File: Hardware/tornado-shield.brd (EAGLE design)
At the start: 84.9 x 84 mm, 32 parts, among them CON1 ROV_SHIELD_V2, Q1 DMP2012SN-7, U1 LM2678S-5.0, U2 LM3409HV'LM3409HV'

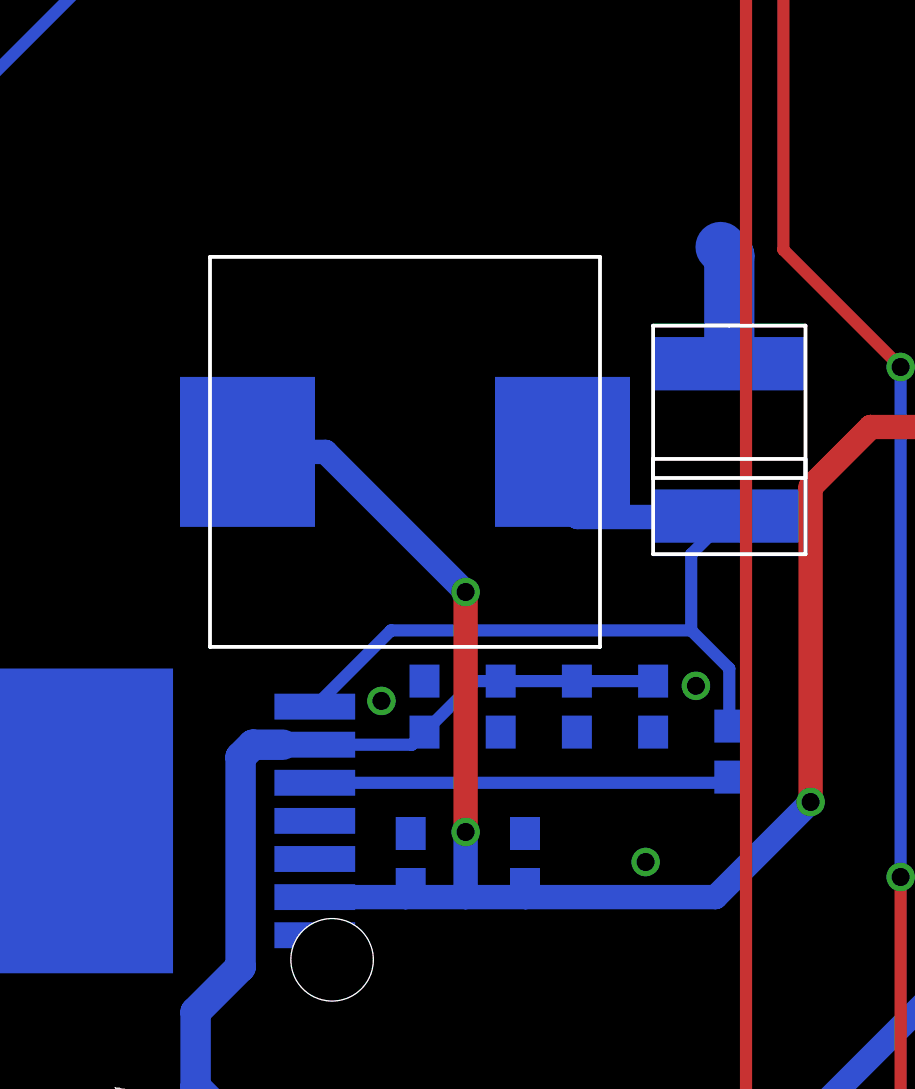
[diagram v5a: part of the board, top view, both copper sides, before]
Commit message: Fixed small problem with buck layout
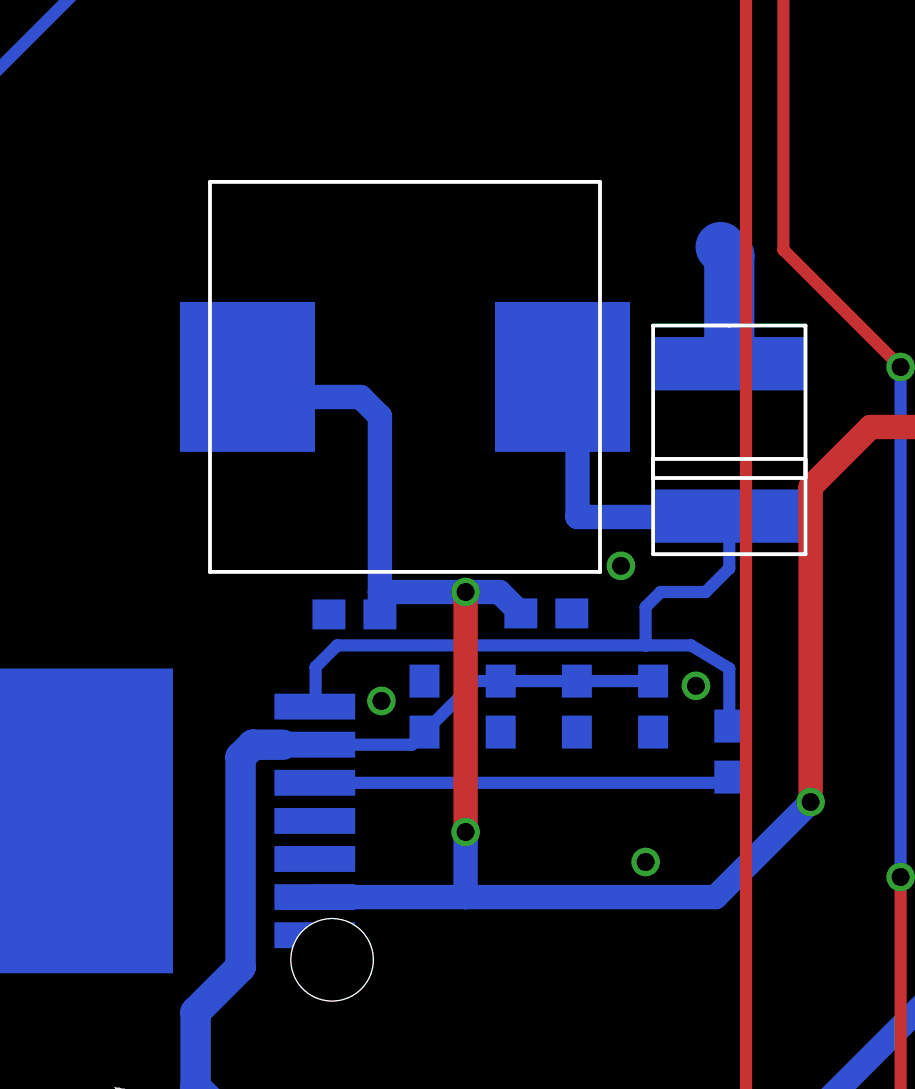
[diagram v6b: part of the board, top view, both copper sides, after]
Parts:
- moved C2 8.37 mm to (21.8, 30.3), turned to 0 degrees
- moved C3 8.22 mm to (28.2, 30.3), turned to 180 degrees
- moved L1 2.50 mm to (23.5, 38.2)
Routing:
- net +5V: track 184.2 -> 190.6 mm
- net SWOUT: track 29.0 -> 34.2 mm
- net GND: vias 6 -> 7
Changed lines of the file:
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@@
 <attribute name="VALUE" x="32.385" y="25.045" size="1.27" layer="28" rot="MR90"/>
 </element>
-<element name="C2" library="rcl" package="C0603" value="180uF" x="23.67" y="22.1" smashed="yes" rot="MR90">
-<attribute name="NAME" x="23.035" y="17.655" size="1.27" layer="26" rot="MR90"/>
-<attribute name="VALUE" x="23.035" y="15.115" size="1.27" layer="28" rot="MR90"/>
-</element>
-<element name="C3" library="rcl" package="C0603" value="180uF" x="27.48" y="22.1" smashed="yes" rot="MR90">
-<attribute name="NAME" x="26.845" y="17.655" size="1.27" layer="26" rot="MR90"/>
-<attribute name="VALUE" x="28.115" y="15.115" size="1.27" layer="28" rot="MR90"/>
+<element name="C2" library="rcl" package="C0603" value="180uF" x="21.79395" y="30.25255" smashed="yes" rot="MR0">
+<attribute name="NAME" x="20.23895" y="29.61755" size="1.27" layer="26" rot="MR0"/>
+<attribute name="VALUE" x="28.77895" y="29.61755" size="1.27" layer="28" rot="MR0"/>
+</element>
+<element name="C3" library="rcl" package="C0603" value="180uF" x="28.18965" y="30.2876" smashed="yes" rot="MR180">
+<attribute name="NAME" x="29.74465" y="30.4226" size="1.27" layer="26" rot="MR180"/>
+<attribute name="VALUE" x="21.20465" y="29.6526" size="1.27" layer="28" rot="MR180"/>
 </element>
 <element name="C4" library="rcl" package="C0603" value="15uF" x="24.13" y="27.18" smashed="yes" rot="MR90">
@@
 </element>
 <element name="C5" library="rcl" package="C0603" value="15uF" x="26.67" y="27.18" smashed="yes" rot="MR270">
-<attribute name="NAME" x="27.305" y="31.625" size="1.27" layer="26" rot="MR270"/>
+<attribute name="NAME" x="25.805" y="25.625" size="1.27" layer="26" rot="MR270"/>
 <attribute name="VALUE" x="26.035" y="32.895" size="1.27" layer="28" rot="MR270"/>
 </element>
 <element name="C6" library="rcl" package="C0603" value="15uF" x="29.21" y="27.18" smashed="yes" rot="MR270">
-<attribute name="NAME" x="29.845" y="31.625" size="1.27" layer="26" rot="MR270"/>
+<attribute name="NAME" x="29.845" y="25.625" size="1.27" layer="26" rot="MR270"/>
 <attribute name="VALUE" x="29.845" y="25.275" size="1.27" layer="28" rot="MR270"/>
 </element>
 <element name="C7" library="rcl" package="C0603" value=".47uF" x="31.75" y="27.18" smashed="yes" rot="MR270">
-<attribute name="NAME" x="32.385" y="31.625" size="1.27" layer="26" rot="MR270"/>
+<attribute name="NAME" x="32.385" y="25.125" size="1.27" layer="26" rot="MR270"/>
 <attribute name="VALUE" x="32.385" y="25.275" size="1.27" layer="28" rot="MR270"/>
 </element>
 <element name="U$3" library="samssuperhot" package="DO-214AB" value="SK1545-TP" x="34.29" y="36.07" smashed="yes" rot="MR270"/>
-<element name="L1" library="samssuperhot" package="7443551221" value="22uH" x="23.48" y="35.67" smashed="yes" rot="MR0"/>
+<element name="L1" library="samssuperhot" package="7443551221" value="22uH" x="23.48" y="38.17" smashed="yes" rot="MR0"/>
 <element name="R_UV2" library="DiscreteComponents" package="R0603" value="13700" x="45.72" y="48.26" smashed="yes" rot="MR180">
 <attribute name="NAME" x="38.1" y="48.895" size="1.27" layer="26" rot="MR180"/>
@@
 <wire x1="34.29" y1="38.61" x2="34.29" y2="42.21" width="1.6764" layer="16"/>
 <wire x1="34.29" y1="42.21" x2="34" y2="42.5" width="1.6764" layer="16"/>
+<via x="30.6778" y="31.873" extent="1-16" drill="0.6"/>
 </signal>
 <signal name="+12V">
@@
 <contactref element="U$3" pad="P$2"/>
 <contactref element="L1" pad="P$1"/>
-<wire x1="20.4724" y1="27.18" x2="23.0124" y2="29.72" width="0.4064" layer="16"/>
-<wire x1="23.0124" y1="29.72" x2="33.02" y2="29.72" width="0.4064" layer="16"/>
-<wire x1="34.29" y1="33.53" x2="33.02" y2="32.26" width="0.4064" layer="16"/>
-<wire x1="33.02" y1="32.26" x2="33.02" y2="29.72" width="0.4064" layer="16"/>
+<wire x1="21.22" y1="29.22" x2="31.5" y2="29.22" width="0.4064" layer="16"/>
+<wire x1="31.5" y1="29.22" x2="33.02" y2="29.22" width="0.4064" layer="16"/>
 <wire x1="34.29" y1="26.53" x2="34.29" y2="28.45" width="0.4064" layer="16"/>
-<wire x1="34.29" y1="28.45" x2="33.02" y2="29.72" width="0.4064" layer="16"/>
-<wire x1="28.73" y1="35.67" x2="29.23" y2="33.5" width="0.8128" layer="16"/>
+<wire x1="34.29" y1="28.45" x2="33.02" y2="29.22" width="0.4064" layer="16"/>
 <wire x1="29.23" y1="33.5" x2="33.5" y2="33.5" width="0.8128" layer="16"/>
 <wire x1="33.5" y1="33.5" x2="33.5" y2="33.53" width="0.8128" layer="16"/>
 <wire x1="33.5" y1="33.53" x2="34.29" y2="33.53" width="0.8128" layer="16"/>
+<wire x1="28.73" y1="38.17" x2="29.23" y2="38.17" width="0.8128" layer="16"/>
+<wire x1="29.23" y1="38.17" x2="29.23" y2="33.5" width="0.8128" layer="16"/>
+<wire x1="21.22" y1="29.22" x2="20.5" y2="28.5" width="0.4064" layer="16"/>
+<wire x1="20.5" y1="28.5" x2="20.5" y2="27.2076" width="0.4064" layer="16"/>
+<wire x1="20.5" y1="27.2076" x2="20.4724" y2="27.18" width="0.4064" layer="16"/>
+<wire x1="34.29" y1="33.53" x2="34.29" y2="31.79" width="0.4064" layer="16"/>
+<wire x1="34.29" y1="31.79" x2="33.5" y2="31" width="0.4064" layer="16"/>
+<wire x1="33.5" y1="31" x2="32" y2="31" width="0.4064" layer="16"/>
+<wire x1="32" y1="31" x2="31.5" y2="30.5" width="0.4064" layer="16"/>
+<wire x1="31.5" y1="30.5" x2="31.5" y2="29.22" width="0.4064" layer="16"/>
 </signal>
 <signal name="+5V">
@@
 <wire x1="81" y1="63.5" x2="82.5" y2="65" width="0.8128" layer="1"/>
 <wire x1="39" y1="36.5" x2="72.5" y2="36.5" width="0.8128" layer="1"/>
-<wire x1="20.4724" y1="20.83" x2="23.5" y2="20.83" width="0.8128" layer="16"/>
-<wire x1="23.5" y1="20.83" x2="25.5" y2="20.83" width="0.8128" layer="16"/>
-<wire x1="25.5" y1="20.83" x2="27.5" y2="20.83" width="0.8128" layer="16"/>
-<wire x1="27.5" y1="20.83" x2="33.83" y2="20.83" width="0.8128" layer="16"/>
+<wire x1="20.4724" y1="20.83" x2="25.5" y2="20.83" width="0.8128" layer="16"/>
+<wire x1="25.5" y1="20.83" x2="33.83" y2="20.83" width="0.8128" layer="16"/>
 <wire x1="33.83" y1="20.83" x2="37" y2="24" width="0.8128" layer="16"/>
 <via x="37" y="24" extent="1-16" drill="0.6"/>
 <wire x1="37" y1="24" x2="37" y2="34.5" width="0.8128" layer="1"/>
 <wire x1="37" y1="34.5" x2="39" y2="36.5" width="0.8128" layer="1"/>
-<wire x1="23.67" y1="21.25" x2="23.67" y2="21" width="0.8128" layer="16"/>
-<wire x1="23.67" y1="21" x2="23.5" y2="20.83" width="0.8128" layer="16"/>
-<wire x1="27.48" y1="21.25" x2="27.48" y2="20.85" width="0.8128" layer="16"/>
-<wire x1="27.48" y1="20.85" x2="27.5" y2="20.83" width="0.8128" layer="16"/>
-<wire x1="18.23" y1="35.67" x2="20.83" y2="35.67" width="0.8128" layer="16"/>
-<wire x1="20.83" y1="35.67" x2="25.5" y2="31" width="0.8128" layer="16"/>
 <via x="25.5" y="31" extent="1-16" drill="0.6"/>
 <wire x1="25.5" y1="31" x2="25.5" y2="23" width="0.8128" layer="1"/>
 <via x="25.5" y="23" extent="1-16" drill="0.6"/>
 <wire x1="25.5" y1="23" x2="25.5" y2="20.83" width="0.8128" layer="16"/>
+<wire x1="25.5" y1="31" x2="22.64395" y2="31" width="0.8128" layer="16"/>
+<wire x1="22.64395" y1="31" x2="22.64395" y2="30.25255" width="0.8128" layer="16"/>
+<wire x1="22.64395" y1="31" x2="22.64395" y2="36.85605" width="0.8128" layer="16"/>
+<wire x1="22.64395" y1="36.85605" x2="22" y2="37.5" width="0.8128" layer="16"/>
+<wire x1="22" y1="37.5" x2="18.9" y2="37.5" width="0.8128" layer="16"/>
+<wire x1="18.9" y1="37.5" x2="18.23" y2="38.17" width="0.8128" layer="16"/>
+<wire x1="27.33965" y1="30.2876" x2="26.62725" y2="31" width="0.8128" layer="16"/>
+<wire x1="26.62725" y1="31" x2="25.5" y2="31" width="0.8128" layer="16"/>
 </signal>
 <signal name="N$2">

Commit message: Added Status LEDs for power and Solenoids
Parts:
- added PWR_ON, SOL1_STAT, SOL2_STAT: (no value), eagle-ltspice:LED_SML0603
- added R3, R4, R5: (no value), rcl:R0603
- R1, R2: device rcl:R1206 -> rcl:R0603
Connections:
- new net N$12: PWR_ON.C, R5.2
- new net N$9: R4.2, SOL1_STAT.C
- new net SOL2_STAT: R3.2, SOL2_STAT.C
- net +5V: now also PWR_ON.A
- net GND: now also R3.1, R4.1, R5.1
- net SOL_O1: now also SOL1_STAT.A
- net SOL_O2: now also SOL2_STAT.A
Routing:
- net +5V: track 190.6 -> 196.7 mm, vias 3 -> 4
- net N$12: track 0.00 -> 4.40 mm, vias 0 -> 1
- net SOL2_STAT: track 0.00 -> 3.79 mm, vias 0 -> 1
- net N$9: track 0.00 -> 3.73 mm, vias 0 -> 1
- net SOL_O1: track 61.8 -> 64.6 mm
- net SOL_O2: track 40.6 -> 42.4 mm
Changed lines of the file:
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@@
 <element name="U$4" library="samssuperhot" package="DO-214AB" value="SK1545-TP" x="11.43" y="55.38" smashed="yes" rot="MR180"/>
 <element name="U$5" library="samssuperhot" package="DO-214AB" value="SK1545-TP" x="11.43" y="70.35" smashed="yes" rot="MR180"/>
-<element name="R2" library="rcl" package="R1206" value="" x="3.81" y="67.31" smashed="yes" rot="MR180">
+<element name="R2" library="rcl" package="R0603" value="" x="3.81" y="67.31" smashed="yes" rot="MR180">
 <attribute name="NAME" x="2.54" y="66.04" size="1.27" layer="26" rot="MR180"/>
 <attribute name="VALUE" x="2.54" y="69.85" size="1.27" layer="28" rot="MR180"/>
 </element>
-<element name="R1" library="rcl" package="R1206" value="" x="3.81" y="54.61" smashed="yes" rot="MR180">
+<element name="R1" library="rcl" package="R0603" value="" x="3.81" y="54.61" smashed="yes" rot="MR180">
 <attribute name="NAME" x="2.54" y="53.34" size="1.27" layer="26" rot="MR180"/>
 <attribute name="VALUE" x="2.54" y="57.15" size="1.27" layer="28" rot="MR180"/>
@@
 <attribute name="VALUE" x="29.595" y="61.365" size="1.27" layer="28" rot="MR90"/>
 </element>
+<element name="PWR_ON" library="eagle-ltspice" package="LED_SML0603" value="" x="27.5" y="16" smashed="yes" rot="R90">
+<attribute name="SPICEPREFIX" value="D" x="27.5" y="16" size="1.778" layer="27" rot="R90" display="off"/>
+<attribute name="SPICETYPE" value="diode" x="27.5" y="16" size="1.778" layer="27" rot="R90" display="off"/>
+<attribute name="SPICEMODEL" value="NONE" x="27.5" y="16" size="1.778" layer="27" rot="R90" display="off"/>
+<attribute name="NAME" x="22" y="13" size="1.27" layer="25"/>
+<attribute name="VALUE" x="29.5" y="15" size="1.27" layer="27" rot="R90"/>
+</element>
+<element name="SOL1_STAT" library="eagle-ltspice" package="LED_SML0603" value="" x="4" y="60.5" smashed="yes" rot="R90">
+<attribute name="SPICEPREFIX" value="D" x="4" y="60.5" size="1.778" layer="27" rot="R90" display="off"/>
+<attribute name="SPICETYPE" value="diode" x="4" y="60.5" size="1.778" layer="27" rot="R90" display="off"/>
+<attribute name="SPICEMODEL" value="NONE" x="4" y="60.5" size="1.778" layer="27" rot="R90" display="off"/>
+<attribute name="NAME" x="3" y="59.5" size="1.27" layer="25" rot="R90"/>
+<attribute name="VALUE" x="6" y="59.5" size="1.27" layer="27" rot="R90"/>
+</element>
+<element name="SOL2_STAT" library="eagle-ltspice" package="LED_SML0603" value="" x="18.5" y="76" smashed="yes" rot="R270">
+<attribute name="SPICEPREFIX" value="D" x="18.5" y="76" size="1.778" layer="27" rot="R270" display="off"/>
+<attribute name="SPICETYPE" value="diode" x="18.5" y="76" size="1.778" layer="27" rot="R270" display="off"/>
+<attribute name="SPICEMODEL" value="NONE" x="18.5" y="76" size="1.778" layer="27" rot="R270" display="off"/>
+<attribute name="NAME" x="14" y="73" size="1.27" layer="25"/>
+<attribute name="VALUE" x="16.5" y="77" size="1.27" layer="27" rot="R270"/>
+</element>
+<element name="R3" library="rcl" package="R0603" value="" x="19" y="79" rot="MR0"/>
+<element name="R4" library="rcl" package="R0603" value="" x="4" y="56.5" rot="MR0"/>
+<element name="R5" library="rcl" package="R0603" value="" x="31" y="13.5" rot="MR0"/>
 </elements>
 <signals>
@@
 <wire x1="34.29" y1="42.21" x2="34" y2="42.5" width="1.6764" layer="16"/>
 <via x="30.6778" y="31.873" extent="1-16" drill="0.6"/>
+<contactref element="R3" pad="1"/>
+<contactref element="R4" pad="1"/>
+<contactref element="R5" pad="1"/>
 </signal>
 <signal name="+12V">
@@
 <wire x1="27.33965" y1="30.2876" x2="26.62725" y2="31" width="0.8128" layer="16"/>
 <wire x1="26.62725" y1="31" x2="25.5" y2="31" width="0.8128" layer="16"/>
+<contactref element="PWR_ON" pad="A"/>
+<wire x1="25.5" y1="20.83" x2="27.5" y2="20.83" width="0.4064" layer="16"/>
+<wire x1="27.5" y1="20.83" x2="27.5" y2="19" width="0.4064" layer="16"/>
+<via x="27.5" y="19" extent="1-16" drill="0.6"/>
+<wire x1="27.5" y1="19" x2="27.5" y2="16.75" width="0.4064" layer="1"/>
 </signal>
 <signal name="N$2">
@@
 <wire x1="8.83" y1="55.88" x2="8.89" y2="55.38" width="0.4064" layer="16"/>
 <wire x1="8.89" y1="55.38" x2="8.89" y2="54.61" width="0.4064" layer="16"/>
-<wire x1="8.89" y1="54.61" x2="5.232" y2="54.61" width="0.4064" layer="16"/>
+<wire x1="8.89" y1="54.61" x2="4.66" y2="54.61" width="0.4064" layer="16"/>
 <wire x1="8.83" y1="61.595" x2="5.905" y2="61.595" width="0.4064" layer="16"/>
 <wire x1="5.905" y1="61.595" x2="4" y2="63.5" width="0.4064" layer="16"/>
@@
 <wire x1="12.5" y1="81.5" x2="32.06" y2="81.5" width="0.4064" layer="1"/>
 <wire x1="32.06" y1="81.5" x2="35.21" y2="78.35" width="0.4064" layer="1"/>
+<contactref element="SOL1_STAT" pad="A"/>
+<wire x1="4" y1="61.25" x2="4" y2="63.5" width="0.4064" layer="1"/>
 </signal>
 <signal name="GPIO2">
@@
 <wire x1="8.83" y1="64.135" x2="6.985" y2="64.135" width="0.4064" layer="16"/>
 <wire x1="6.985" y1="64.135" x2="5.232" y2="65.888" width="0.4064" layer="16"/>
-<wire x1="5.232" y1="65.888" x2="5.232" y2="67.31" width="0.4064" layer="16"/>
-<wire x1="5.232" y1="67.31" x2="7.772" y2="69.85" width="0.4064" layer="16"/>
+<wire x1="5.232" y1="65.888" x2="4.66" y2="67.31" width="0.4064" layer="16"/>
+<wire x1="4.66" y1="67.31" x2="7.772" y2="69.85" width="0.4064" layer="16"/>
 <wire x1="7.772" y1="69.85" x2="8.89" y2="70.35" width="0.4064" layer="16"/>
 <wire x1="8.89" y1="70.35" x2="8.89" y2="72.89" width="0.4064" layer="16"/>
 <wire x1="8.89" y1="72.89" x2="10" y2="74" width="0.4064" layer="16"/>
 <via x="10" y="74" extent="1-16" drill="0.6"/>
-<wire x1="10" y1="74" x2="33.4" y2="74" width="0.4064" layer="1"/>
+<wire x1="10" y1="74" x2="18.5" y2="74" width="0.4064" layer="1"/>
+<wire x1="18.5" y1="74" x2="33.4" y2="74" width="0.4064" layer="1"/>
 <wire x1="33.4" y1="74" x2="35.21" y2="75.81" width="0.4064" layer="1"/>
+<contactref element="SOL2_STAT" pad="A"/>
+<wire x1="18.5" y1="75.25" x2="18.5" y2="74" width="0.4064" layer="1"/>
 </signal>
 <signal name="GPIO3">
@@
 <signal name="N$6">
 </signal>
+<signal name="SOL2_STAT">
+<contactref element="SOL2_STAT" pad="C"/>
+<contactref element="R3" pad="2"/>
+<wire x1="18.5" y1="76.75" x2="17.75" y2="76.75" width="0.4064" layer="1"/>
+<wire x1="17.75" y1="76.75" x2="17" y2="77.5" width="0.4064" layer="1"/>
+<wire x1="18.15" y1="79" x2="17" y2="77.85" width="0.4064" layer="16"/>
+<wire x1="17" y1="77.85" x2="17" y2="77.5" width="0.4064" layer="16"/>
+<wire x1="17" y1="77.5" x2="17" y2="77.5" width="0" layer="19" extent="1-16"/>
+<via x="17" y="77.5" extent="1-16" drill="0.6"/>
+</signal>
+<signal name="N$12">
+<contactref element="PWR_ON" pad="C"/>
+<contactref element="R5" pad="2"/>
+<wire x1="27.5" y1="15.25" x2="30" y2="15.25" width="0.4064" layer="1"/>
+<wire x1="30" y1="15.25" x2="30" y2="15" width="0.4064" layer="1"/>
+<via x="30" y="15" extent="1-16" drill="0.6"/>
+<wire x1="30" y1="15" x2="30.15" y2="15" width="0.4064" layer="16"/>
+<wire x1="30.15" y1="15" x2="30.15" y2="13.5" width="0.4064" layer="16"/>
+</signal>
+<signal name="N$9">
+<contactref element="SOL1_STAT" pad="C"/>
+<contactref element="R4" pad="2"/>
+<wire x1="4" y1="59.75" x2="3" y2="58.75" width="0.4064" layer="1"/>
+<wire x1="3" y1="58.75" x2="3" y2="58.5" width="0.4064" layer="1"/>
+<via x="3" y="58.5" extent="1-16" drill="0.6"/>
+<wire x1="3" y1="58.5" x2="3.15" y2="58.35" width="0.4064" layer="16"/>
+<wire x1="3.15" y1="58.35" x2="3.15" y2="56.5" width="0.4064" layer="16"/>
+</signal>
 </signals>
